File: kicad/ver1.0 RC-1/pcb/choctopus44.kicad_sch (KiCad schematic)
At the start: 102 parts, among them SW1 SW_PUSH, SW10 SW_PUSH, SW11 SW_PUSH, SW12 SW_PUSH, SW13 SW_PUSH, SW14 SW_PUSH, SW15 SW_PUSH, SW16 SW_PUSH, SW17 SW_PUSH, SW18 SW_PUSH, SW19 SW_PUSH, SW2 SW_PUSH, SW20 SW_PUSH, SW21 SW_PUSH, SW22 SW_PUSH, SW23 SW_PUSH, SW24 SW_PUSH, SW25 SW_PUSH, SW26 SW_PUSH, SW27 SW_PUSH, SW28 SW_PUSH, SW29 SW_PUSH, SW3 SW_PUSH, SW30 SW_PUSH, SW31 SW_PUSH, SW32 SW_PUSH, SW33 SW_PUSH, SW34 SW_PUSH, SW35 SW_PUSH, SW36 SW_PUSH, SW37 SW_PUSH, SW38 SW_PUSH, SW39 SW_PUSH, SW4 SW_PUSH, SW40 SW_PUSH, SW41 SW_PUSH, SW42 SW_PUSH, SW43 SW_PUSH, SW44 SW_PUSH, SW45 Rotary_Encoder_Switch, SW5 SW_PUSH, SW6 SW_PUSH, SW7 SW_PUSH, SW8 SW_PUSH, SW9 SW_PUSH, U1 ProMicro/Nice!Nano

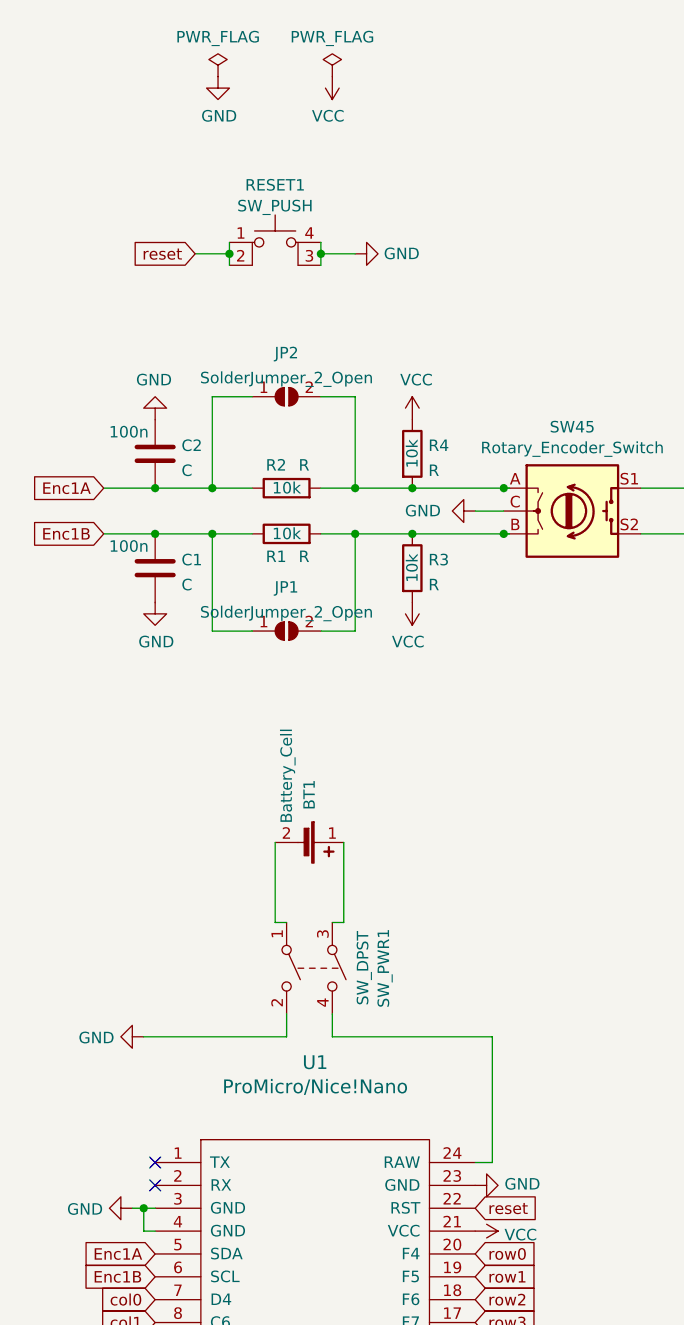
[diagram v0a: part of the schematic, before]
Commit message: revise power and reset circuits
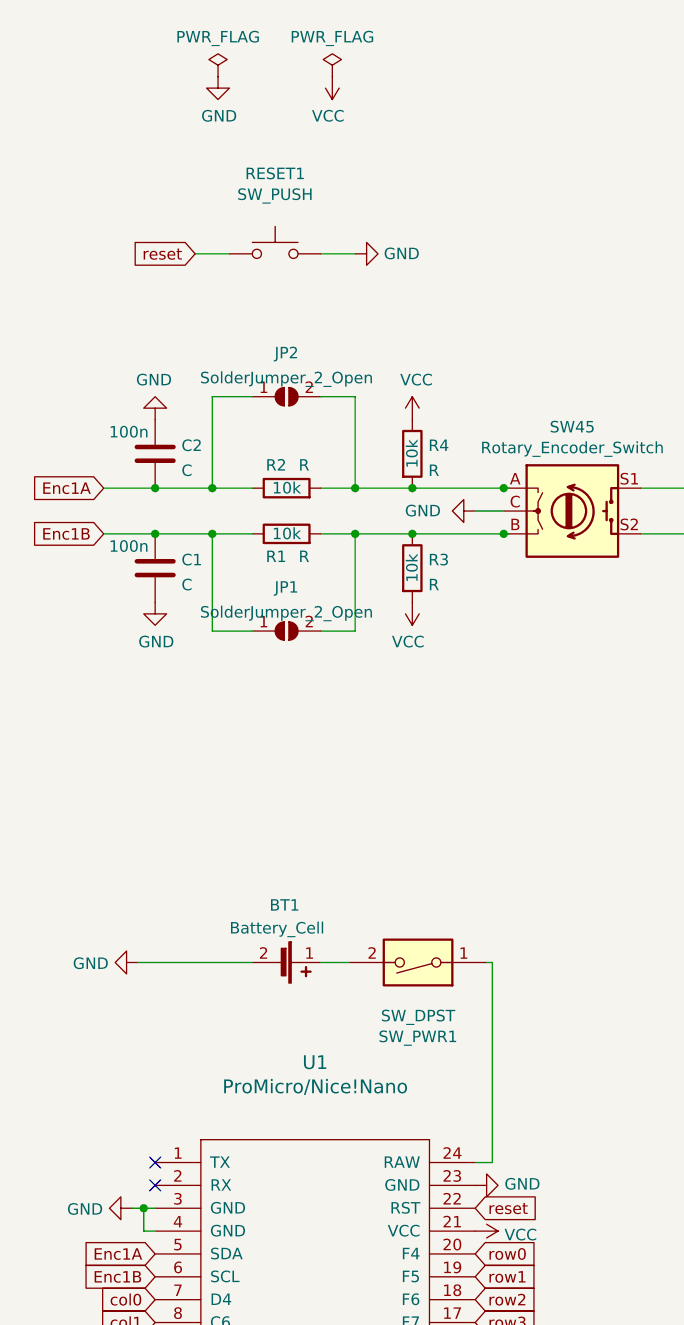
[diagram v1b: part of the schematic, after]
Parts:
- RESET1: footprint Button_Switch_THT:SW_TH_Tactile_Omron_B3F-10xx -> Button_Switch_SMD:SW_SPST_TL3342; symbol Switch:SW_MEC_5E -> Switch:SW_Push
- SW_PWR1: footprint Button_Switch_THT:SW_E-Switch_EG1271_DPDT -> Button_Switch_SMD:SW_SPDT_PCM12; symbol Switch:SW_DPST -> Switch:SW_DIP_x01
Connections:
- net GND: now also BT1.2 (-), RESET1.2; no longer RESET1.3 (K), RESET1.4 (A), SW_PWR1.2
- net reset: no longer RESET1.2
- net at U1.24 (RAW): now also SW_PWR1.1; no longer SW_PWR1.4
- net at BT1.1 (+): now also SW_PWR1.2; no longer SW_PWR1.3
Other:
- moved on the sheet: BT1
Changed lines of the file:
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@@
   (junction (at 163.195 115.57) (diameter 0) (color 0 0 0 0)
   )
-  (junction (at 60.96 50.8) (diameter 0) (color 0 0 0 0)
-  )
   (junction (at 178.435 89.535) (diameter 0) (color 0 0 0 0)
   )
@@
   (junction (at 163.195 48.895) (diameter 0) (color 0 0 0 0)
   )
-  (junction (at 50.8 50.8) (diameter 0) (color 0 0 0 0)
-  )
   (junction (at 188.595 65.405) (diameter 0) (color 0 0 0 0)
   )
@@
     (stroke (width 0) (type default) (color 0 0 0 0))
   )
-  (wire (pts (xy 63.5 125.095) (xy 62.23 125.095))
-    (stroke (width 0) (type default) (color 0 0 0 0))
-  )
   (wire (pts (xy 213.995 24.765) (xy 213.995 32.385))
     (stroke (width 0) (type default) (color 0 0 0 0))
@@
     (stroke (width 0) (type default) (color 0 0 0 0))
   )
+  (wire (pts (xy 60.96 129.54) (xy 64.135 129.54))
+    (stroke (width 0) (type default) (color 0 0 0 0))
+  )
   (wire (pts (xy 81.28 76.835) (xy 81.915 76.835))
     (stroke (width 0) (type default) (color 0 0 0 0))
@@
     (stroke (width 0) (type default) (color 0 0 0 0))
   )
-  (wire (pts (xy 57.15 135.255) (xy 57.15 137.795))
-    (stroke (width 0) (type default) (color 0 0 0 0))
-  )
-  (wire (pts (xy 50.8 50.8) (xy 50.8 52.07))
-    (stroke (width 0) (type default) (color 0 0 0 0))
-  )
   (wire (pts (xy 203.835 81.915) (xy 201.295 81.915))
     (stroke (width 0) (type default) (color 0 0 0 0))
@@
     (stroke (width 0) (type default) (color 0 0 0 0))
   )
-  (wire (pts (xy 55.88 116.205) (xy 55.88 125.095))
-    (stroke (width 0) (type default) (color 0 0 0 0))
-  )
   (wire (pts (xy 80.01 151.765) (xy 78.105 151.765))
     (stroke (width 0) (type default) (color 0 0 0 0))
@@
     (stroke (width 0) (type default) (color 0 0 0 0))
   )
-  (wire (pts (xy 50.8 49.53) (xy 50.8 50.8))
-    (stroke (width 0) (type default) (color 0 0 0 0))
-  )
   (wire (pts (xy 254.635 65.405) (xy 252.095 65.405))
     (stroke (width 0) (type default) (color 0 0 0 0))
@@
     (stroke (width 0) (type default) (color 0 0 0 0))
   )
-  (wire (pts (xy 57.15 137.795) (xy 41.275 137.795))
-    (stroke (width 0) (type default) (color 0 0 0 0))
-  )
   (wire (pts (xy 153.035 123.19) (xy 178.435 123.19))
     (stroke (width 0) (type default) (color 0 0 0 0))
@@
     (stroke (width 0) (type default) (color 0 0 0 0))
   )
-  (wire (pts (xy 55.88 125.095) (xy 57.15 125.095))
-    (stroke (width 0) (type default) (color 0 0 0 0))
-  )
   (wire (pts (xy 229.235 56.515) (xy 254.635 56.515))
     (stroke (width 0) (type default) (color 0 0 0 0))
@@
     (stroke (width 0) (type default) (color 0 0 0 0))
   )
-  (wire (pts (xy 80.01 137.795) (xy 80.01 151.765))
+  (wire (pts (xy 80.01 129.54) (xy 80.01 151.765))
     (stroke (width 0) (type default) (color 0 0 0 0))
   )
@@
     (stroke (width 0) (type default) (color 0 0 0 0))
   )
+  (wire (pts (xy 40.64 129.54) (xy 53.34 129.54))
+    (stroke (width 0) (type default) (color 0 0 0 0))
+  )
   (wire (pts (xy 137.795 99.06) (xy 137.795 115.57))
     (stroke (width 0) (type default) (color 0 0 0 0))
@@
     (stroke (width 0) (type default) (color 0 0 0 0))
   )
-  (wire (pts (xy 62.23 135.255) (xy 62.23 137.795))
-    (stroke (width 0) (type default) (color 0 0 0 0))
-  )
   (wire (pts (xy 153.035 40.005) (xy 178.435 40.005))
     (stroke (width 0) (type default) (color 0 0 0 0))
@@
     (stroke (width 0) (type default) (color 0 0 0 0))
   )
+  (wire (pts (xy 80.01 129.54) (xy 79.375 129.54))
+    (stroke (width 0) (type default) (color 0 0 0 0))
+  )
   (wire (pts (xy 163.195 149.225) (xy 165.735 149.225))
     (stroke (width 0) (type default) (color 0 0 0 0))
@@
     (stroke (width 0) (type default) (color 0 0 0 0))
   )
-  (wire (pts (xy 62.23 137.795) (xy 80.01 137.795))
-    (stroke (width 0) (type default) (color 0 0 0 0))
-  )
   (wire (pts (xy 150.495 132.08) (xy 153.035 132.08))
     (stroke (width 0) (type default) (color 0 0 0 0))
@@
     (stroke (width 0) (type default) (color 0 0 0 0))
   )
-  (wire (pts (xy 60.96 50.8) (xy 60.96 52.07))
-    (stroke (width 0) (type default) (color 0 0 0 0))
-  )
   (wire (pts (xy 239.395 24.765) (xy 239.395 32.385))
     (stroke (width 0) (type default) (color 0 0 0 0))
@@
     (stroke (width 0) (type default) (color 0 0 0 0))
   )
-  (wire (pts (xy 63.5 116.205) (xy 63.5 125.095))
-    (stroke (width 0) (type default) (color 0 0 0 0))
-  )
   (wire (pts (xy 178.435 106.68) (xy 203.835 106.68))
     (stroke (width 0) (type default) (color 0 0 0 0))
@@
     (stroke (width 0) (type default) (color 0 0 0 0))
   )
-  (wire (pts (xy 60.96 49.53) (xy 60.96 50.8))
-    (stroke (width 0) (type default) (color 0 0 0 0))
-  )
   (wire (pts (xy 239.395 99.06) (xy 241.935 99.06))
     (stroke (width 0) (type default) (color 0 0 0 0))
@@
     (pin "2")
   )
-  (symbol (lib_id "Switch:SW_MEC_5E") (at 55.88 52.07 0) (unit 1)
+  (symbol (lib_id "Switch:SW_Push") (at 55.88 50.8 0) (unit 1)
     (in_bom yes) (on_board yes)
-    (property "Reference" "RESET1" (id 0) (at 55.88 43.18 0))
-    (property "Value" "SW_PUSH" (id 1) (at 55.88 45.4914 0))
-    (property "Footprint" "Button_Switch_THT:SW_TH_Tactile_Omron_B3F-10xx" (id 2) (at 55.88 44.45 0)
+    (property "Reference" "RESET1" (id 0) (at 55.88 41.91 0))
+    (property "Value" "SW_PUSH" (id 1) (at 55.88 44.2214 0))
+    (property "Footprint" "Button_Switch_SMD:SW_SPST_TL3342" (id 2) (at 55.88 45.72 0)
       (effects (font (size 1.27 1.27)) hide)
     )
-    (property "Datasheet" "http://www.apem.com/int/index.php?controller=attachment&id_attachment=1371" (id 3) (at 55.88 44.45 0)
+    (property "Datasheet" "~" (id 3) (at 55.88 45.72 0)
       (effects (font (size 1.27 1.27)) hide)
     )
     (pin "1")
     (pin "2")
-    (pin "3")
-    (pin "4")
   )
   (symbol (lib_id "power:GND") (at 64.77 50.8 90) (unit 1)
@@
     (pin "2")
   )
-  (symbol (lib_id "Switch:SW_DPST") (at 59.69 130.175 270) (unit 1)
+  (symbol (lib_id "Switch:SW_DIP_x01") (at 71.755 129.54 180) (unit 1)
     (in_bom yes) (on_board yes)
-    (property "Reference" "SW_PWR1" (id 0) (at 67.945 130.175 0))
-    (property "Value" "SW_DPST" (id 1) (at 65.6336 130.175 0))
-    (property "Footprint" "Button_Switch_THT:SW_E-Switch_EG1271_DPDT" (id 2) (at 59.69 130.175 0)
+    (property "Reference" "SW_PWR1" (id 0) (at 71.755 137.795 0))
+    (property "Value" "SW_DPST" (id 1) (at 71.755 135.4836 0))
+    (property "Footprint" "Button_Switch_SMD:SW_SPDT_PCM12" (id 2) (at 71.755 129.54 0)
       (effects (font (size 1.27 1.27)) hide)
     )
-    (property "Datasheet" "~" (id 3) (at 59.69 130.175 0)
+    (property "Datasheet" "~" (id 3) (at 71.755 129.54 0)
       (effects (font (size 1.27 1.27)) hide)
     )
     (pin "1")
     (pin "2")
-    (pin "3")
-    (pin "4")
   )
-  (symbol (lib_id "Device:Battery_Cell") (at 58.42 116.205 270) (unit 1)
+  (symbol (lib_id "Device:Battery_Cell") (at 55.88 129.54 270) (unit 1)
     (in_bom yes) (on_board yes)
-    (property "Reference" "BT1" (id 0) (at 59.69 109.22 0)
+    (property "Reference" "BT1" (id 0) (at 55.245 123.19 90)
       (effects (font (size 1.27 1.27)) (justify left))
     )
-    (property "Value" "Battery_Cell" (id 1) (at 57.15 103.505 0)
+    (property "Value" "Battery_Cell" (id 1) (at 50.8 125.73 90)
       (effects (font (size 1.27 1.27)) (justify left))
     )
-    (property "Footprint" "Connector_PinHeader_2.00mm:PinHeader_1x02_P2.00mm_Vertical" (id 2) (at 59.944 116.205 90)
+    (property "Footprint" "Connector_PinHeader_2.00mm:PinHeader_1x02_P2.00mm_Vertical" (id 2) (at 57.404 129.54 90)
       (effects (font (size 1.27 1.27)) hide)
     )
-    (property "Datasheet" "~" (id 3) (at 59.944 116.205 90)
+    (property "Datasheet" "~" (id 3) (at 57.404 129.54 90)
       (effects (font (size 1.27 1.27)) hide)
     )
@@
     (pin "2")
   )
-  (symbol (lib_id "power:GND") (at 41.275 137.795 270) (unit 1)
+  (symbol (lib_id "power:GND") (at 40.64 129.54 270) (unit 1)
     (in_bom yes) (on_board yes)
-    (property "Reference" "#PWR0104" (id 0) (at 34.925 137.795 0)
+    (property "Reference" "#PWR0104" (id 0) (at 34.29 129.54 0)
       (effects (font (size 1.27 1.27)) hide)
     )
-    (property "Value" "GND" (id 1) (at 38.0238 137.922 90)
+    (property "Value" "GND" (id 1) (at 37.3888 129.667 90)
       (effects (font (size 1.27 1.27)) (justify right))
     )
-    (property "Footprint" "" (id 2) (at 41.275 137.795 0)
+    (property "Footprint" "" (id 2) (at 40.64 129.54 0)
       (effects (font (size 1.27 1.27)) hide)
     )
-    (property "Datasheet" "" (id 3) (at 41.275 137.795 0)
+    (property "Datasheet" "" (id 3) (at 40.64 129.54 0)
       (effects (font (size 1.27 1.27)) hide)
     )
@@
     )
     (path "/00000000-0000-0000-0000-00005dd41146"
-      (reference "RESET1") (unit 1) (value "SW_PUSH") (footprint "Button_Switch_THT:SW_TH_Tactile_Omron_B3F-10xx")
+      (reference "RESET1") (unit 1) (value "SW_PUSH") (footprint "Button_Switch_SMD:SW_SPST_TL3342")
     )
     (path "/00000000-0000-0000-0000-00005dcbd08b"
@@
     )
     (path "/00000000-0000-0000-0000-000060df3383"
-      (reference "SW_PWR1") (unit 1) (value "SW_DPST") (footprint "Button_Switch_THT:SW_E-Switch_EG1271_DPDT")
+      (reference "SW_PWR1") (unit 1) (value "SW_DPST") (footprint "Button_Switch_SMD:SW_SPDT_PCM12")
     )
     (path "/00000000-0000-0000-0000-00005dcbb133"

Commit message: revise encoder area
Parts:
- C1, C2: footprint custom-electronics:Dual-Hybrid-1206-C_Disc_D4.3mm_W1.9mm_P5.00mm -> custom-electronics:1206_hybrid
- JP1, JP2: footprint Jumper:SolderJumper-2_P1.3mm_Open_Pad1.0x1.5mm -> Jumper:SolderJumper-2_P1.3mm_Open_TrianglePad1.0x1.5mm
- R1, R2, R3, R4: footprint Resistor_THT:R_Axial_DIN0204_L3.6mm_D1.6mm_P7.62mm_Horizontal -> custom-electronics:1206_hybrid
- SW_PWR1: symbol Switch:SW_DIP_x01 -> Switch:SW_SPDT
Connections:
- no-connect marks 2 -> 3
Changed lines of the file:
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@@
   (junction (at 188.595 81.915) (diameter 0) (color 0 0 0 0)
   )
+  (no_connect (at 74.295 132.08))
   (no_connect (at 42.545 151.765))
   (no_connect (at 42.545 154.305))
@@
     (stroke (width 0) (type default) (color 0 0 0 0))
   )
+  (wire (pts (xy 80.01 127) (xy 74.295 127))
+    (stroke (width 0) (type default) (color 0 0 0 0))
+  )
   (wire (pts (xy 254.635 115.57) (xy 252.095 115.57))
     (stroke (width 0) (type default) (color 0 0 0 0))
@@
     (stroke (width 0) (type default) (color 0 0 0 0))
   )
-  (wire (pts (xy 80.01 129.54) (xy 80.01 151.765))
-    (stroke (width 0) (type default) (color 0 0 0 0))
-  )
   (wire (pts (xy 213.995 32.385) (xy 213.995 48.895))
     (stroke (width 0) (type default) (color 0 0 0 0))
@@
     (stroke (width 0) (type default) (color 0 0 0 0))
   )
+  (wire (pts (xy 80.01 127) (xy 80.01 151.765))
+    (stroke (width 0) (type default) (color 0 0 0 0))
+  )
   (wire (pts (xy 64.77 66.675) (xy 64.77 76.835))
     (stroke (width 0) (type default) (color 0 0 0 0))
@@
   )
   (wire (pts (xy 203.835 106.68) (xy 229.235 106.68))
-    (stroke (width 0) (type default) (color 0 0 0 0))
-  )
-  (wire (pts (xy 80.01 129.54) (xy 79.375 129.54))
     (stroke (width 0) (type default) (color 0 0 0 0))
   )
@@
     (pin "2")
   )
-  (symbol (lib_id "Switch:SW_DIP_x01") (at 71.755 129.54 180) (unit 1)
-    (in_bom yes) (on_board yes)
-    (property "Reference" "SW_PWR1" (id 0) (at 71.755 137.795 0))
-    (property "Value" "SW_DPST" (id 1) (at 71.755 135.4836 0))
-    (property "Footprint" "Button_Switch_SMD:SW_SPDT_PCM12" (id 2) (at 71.755 129.54 0)
-      (effects (font (size 1.27 1.27)) hide)
-    )
-    (property "Datasheet" "~" (id 3) (at 71.755 129.54 0)
-      (effects (font (size 1.27 1.27)) hide)
-    )
-    (pin "1")
-    (pin "2")
+  (symbol (lib_id "Switch:SW_SPDT") (at 69.215 129.54 0) (unit 1)
+    (in_bom yes) (on_board yes)
+    (property "Reference" "SW_PWR1" (id 0) (at 69.215 121.285 0))
+    (property "Value" "SW_DPST" (id 1) (at 69.215 123.5964 0))
+    (property "Footprint" "Button_Switch_SMD:SW_SPDT_PCM12" (id 2) (at 69.215 129.54 0)
+      (effects (font (size 1.27 1.27)) hide)
+    )
+    (property "Datasheet" "~" (id 3) (at 69.215 129.54 0)
+      (effects (font (size 1.27 1.27)) hide)
+    )
+    (pin "1")
+    (pin "2")
+    (pin "3")
   )
   (symbol (lib_id "Device:Battery_Cell") (at 55.88 129.54 270) (unit 1)
@@
       (effects (font (size 1.27 1.27)) (justify left))
     )
-    (property "Footprint" "Resistor_THT:R_Axial_DIN0204_L3.6mm_D1.6mm_P7.62mm_Horizontal" (id 2) (at 57.15 78.613 90)
+    (property "Footprint" "custom-electronics:1206_hybrid" (id 2) (at 57.15 78.613 90)
       (effects (font (size 1.27 1.27)) hide)
     )
@@
       (effects (font (size 1.27 1.27)) (justify left))
     )
-    (property "Footprint" "Resistor_THT:R_Axial_DIN0204_L3.6mm_D1.6mm_P7.62mm_Horizontal" (id 2) (at 69.342 85.725 90)
+    (property "Footprint" "custom-electronics:1206_hybrid" (id 2) (at 69.342 85.725 90)
       (effects (font (size 1.27 1.27)) hide)
     )
@@
     (property "Reference" "JP1" (id 0) (at 57.15 87.8545 0))
     (property "Value" "SolderJumper_2_Open" (id 1) (at 57.15 90.6296 0))
-    (property "Footprint" "Jumper:SolderJumper-2_P1.3mm_Open_Pad1.0x1.5mm" (id 2) (at 57.15 92.71 0)
+    (property "Footprint" "Jumper:SolderJumper-2_P1.3mm_Open_TrianglePad1.0x1.5mm" (id 2) (at 57.15 92.71 0)
       (effects (font (size 1.27 1.27)) hide)
     )
@@
       (effects (font (size 1.27 1.27)) (justify left))
     )
-    (property "Footprint" "Resistor_THT:R_Axial_DIN0204_L3.6mm_D1.6mm_P7.62mm_Horizontal" (id 2) (at 69.342 73.025 90)
+    (property "Footprint" "custom-electronics:1206_hybrid" (id 2) (at 69.342 73.025 90)
       (effects (font (size 1.27 1.27)) hide)
     )
@@
       (effects (font (size 1.27 1.27)) (justify left))
     )
-    (property "Footprint" "custom-electronics:Dual-Hybrid-1206-C_Disc_D4.3mm_W1.9mm_P5.00mm" (id 2) (at 43.5102 89.535 0)
+    (property "Footprint" "custom-electronics:1206_hybrid" (id 2) (at 43.5102 89.535 0)
       (effects (font (size 1.27 1.27)) hide)
     )
@@
       (effects (font (size 1.27 1.27)) (justify left))
     )
-    (property "Footprint" "custom-electronics:Dual-Hybrid-1206-C_Disc_D4.3mm_W1.9mm_P5.00mm" (id 2) (at 43.5102 76.835 0)
+    (property "Footprint" "custom-electronics:1206_hybrid" (id 2) (at 43.5102 76.835 0)
       (effects (font (size 1.27 1.27)) hide)
     )
@@
       (effects (font (size 1.27 1.27)) (justify left))
     )
-    (property "Footprint" "Resistor_THT:R_Axial_DIN0204_L3.6mm_D1.6mm_P7.62mm_Horizontal" (id 2) (at 57.15 83.693 90)
+    (property "Footprint" "custom-electronics:1206_hybrid" (id 2) (at 57.15 83.693 90)
       (effects (font (size 1.27 1.27)) hide)
     )
@@
     (property "Reference" "JP2" (id 0) (at 57.15 61.8195 0))
     (property "Value" "SolderJumper_2_Open" (id 1) (at 57.15 64.5946 0))
-    (property "Footprint" "Jumper:SolderJumper-2_P1.3mm_Open_Pad1.0x1.5mm" (id 2) (at 57.15 66.675 0)
+    (property "Footprint" "Jumper:SolderJumper-2_P1.3mm_Open_TrianglePad1.0x1.5mm" (id 2) (at 57.15 66.675 0)
       (effects (font (size 1.27 1.27)) hide)
     )
@@
     )
     (path "/a75a6b6e-fd3e-4beb-a876-b0db64cea578"
-      (reference "C1") (unit 1) (value "C") (footprint "custom-electronics:Dual-Hybrid-1206-C_Disc_D4.3mm_W1.9mm_P5.00mm")
+      (reference "C1") (unit 1) (value "C") (footprint "custom-electronics:1206_hybrid")
     )
     (path "/d44f6aaa-f8db-4ae4-8055-30867637d971"
-      (reference "C2") (unit 1) (value "C") (footprint "custom-electronics:Dual-Hybrid-1206-C_Disc_D4.3mm_W1.9mm_P5.00mm")
+      (reference "C2") (unit 1) (value "C") (footprint "custom-electronics:1206_hybrid")
     )
     (path "/00000000-0000-0000-0000-00005dcbd469"
@@
     )
     (path "/5addf36d-27f5-4b24-afb8-bb75d47ace2f"
-      (reference "JP1") (unit 1) (value "SolderJumper_2_Open") (footprint "Jumper:SolderJumper-2_P1.3mm_Open_Pad1.0x1.5mm")
+      (reference "JP1") (unit 1) (value "SolderJumper_2_Open") (footprint "Jumper:SolderJumper-2_P1.3mm_Open_TrianglePad1.0x1.5mm")
     )
     (path "/ea622771-3cf0-4c6c-863e-6326c4f96725"
-      (reference "JP2") (unit 1) (value "SolderJumper_2_Open") (footprint "Jumper:SolderJumper-2_P1.3mm_Open_Pad1.0x1.5mm")
+      (reference "JP2") (unit 1) (value "SolderJumper_2_Open") (footprint "Jumper:SolderJumper-2_P1.3mm_Open_TrianglePad1.0x1.5mm")
     )
     (path "/e05e05eb-3836-476f-a11a-aebc6024e210"
-      (reference "R1") (unit 1) (value "R") (footprint "Resistor_THT:R_Axial_DIN0204_L3.6mm_D1.6mm_P7.62mm_Horizontal")
+      (reference "R1") (unit 1) (value "R") (footprint "custom-electronics:1206_hybrid")
     )
     (path "/327a37f4-3106-46a4-bcc5-c91beff31d2f"
-      (reference "R2") (unit 1) (value "R") (footprint "Resistor_THT:R_Axial_DIN0204_L3.6mm_D1.6mm_P7.62mm_Horizontal")
+      (reference "R2") (unit 1) (value "R") (footprint "custom-electronics:1206_hybrid")
     )
     (path "/500b6bb3-8f59-48b4-bea8-02d8b26ebe96"
-      (reference "R3") (unit 1) (value "R") (footprint "Resistor_THT:R_Axial_DIN0204_L3.6mm_D1.6mm_P7.62mm_Horizontal")
+      (reference "R3") (unit 1) (value "R") (footprint "custom-electronics:1206_hybrid")
     )
     (path "/8c257c1a-38e6-428d-b87b-83ace65ac5d4"
-      (reference "R4") (unit 1) (value "R") (footprint "Resistor_THT:R_Axial_DIN0204_L3.6mm_D1.6mm_P7.62mm_Horizontal")
+      (reference "R4") (unit 1) (value "R") (footprint "custom-electronics:1206_hybrid")
     )
     (path "/00000000-0000-0000-0000-00005dd41146"
